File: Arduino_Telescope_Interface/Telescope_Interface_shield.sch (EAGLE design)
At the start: 30 parts, among them IC1 40106N, IC2 24LC256P, J1 RJ45, J11 455-1750-1-ND, J12 455-1750-1-ND, J4 455-1750-1-ND, J8 455-1750-1-ND, J9 455-1750-1-ND, SW2 MOMENTARY-SWITCH-SPST-PTH-6.0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

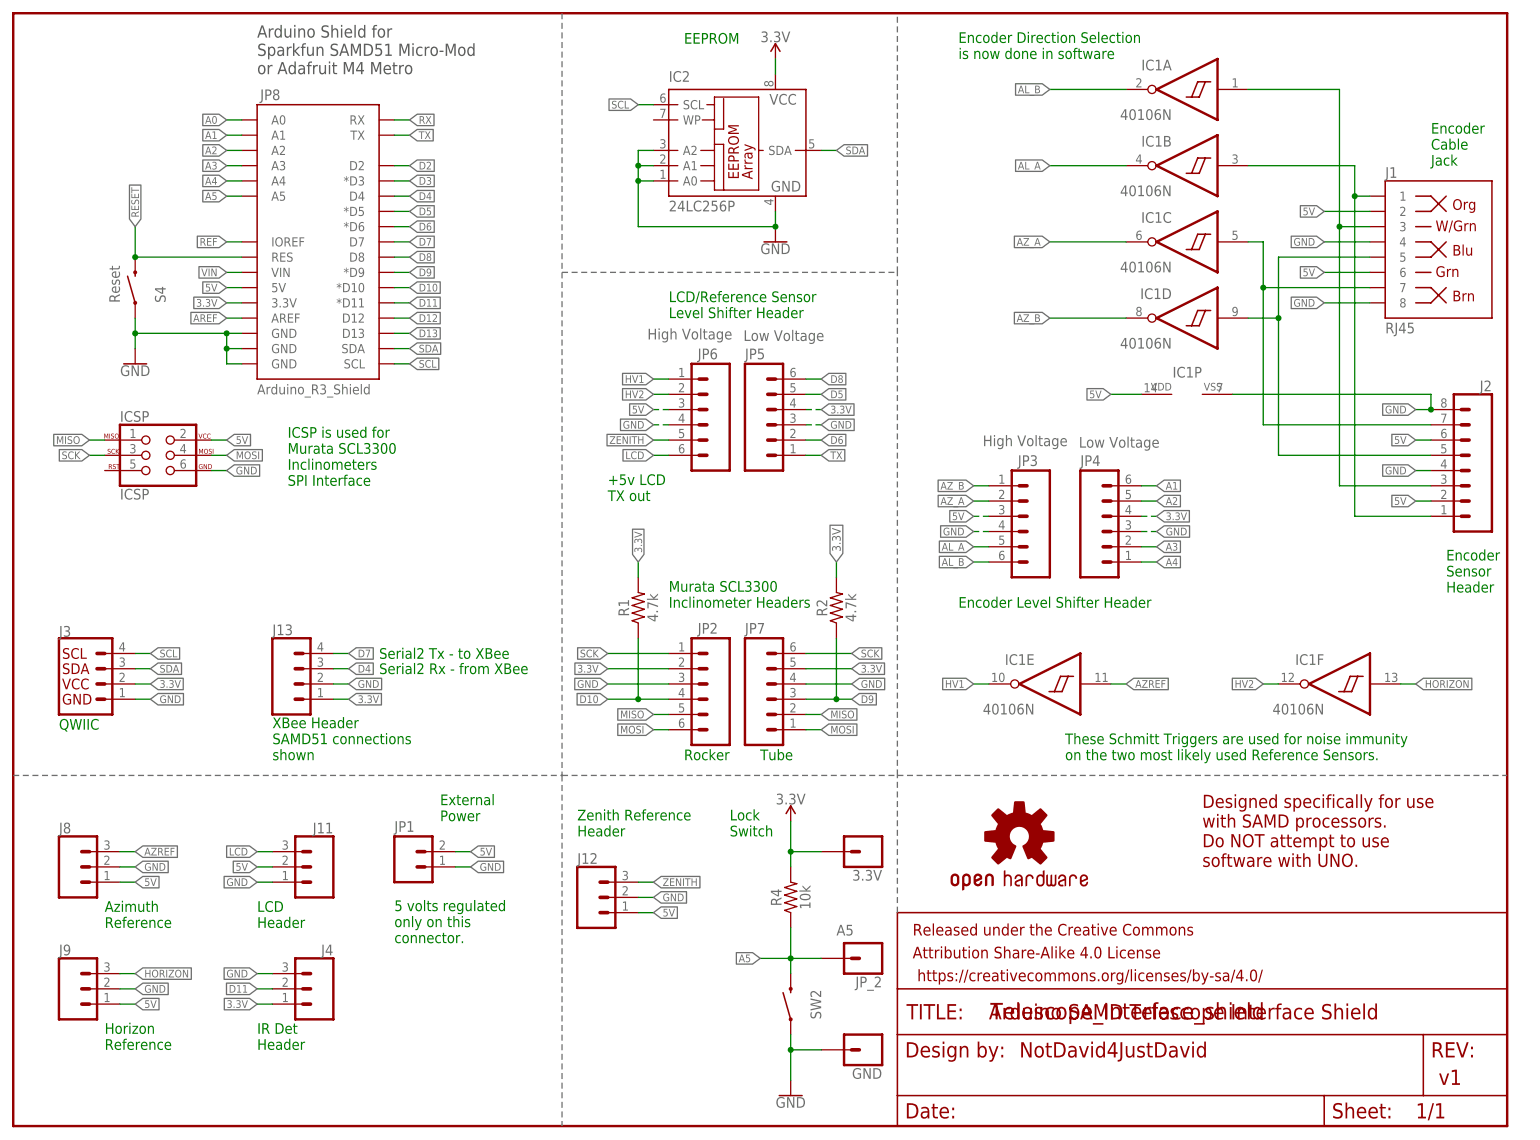
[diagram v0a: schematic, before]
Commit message: latest  changes in design, etc
Update design to separate out power monitoring.  Lots of other stuff too.
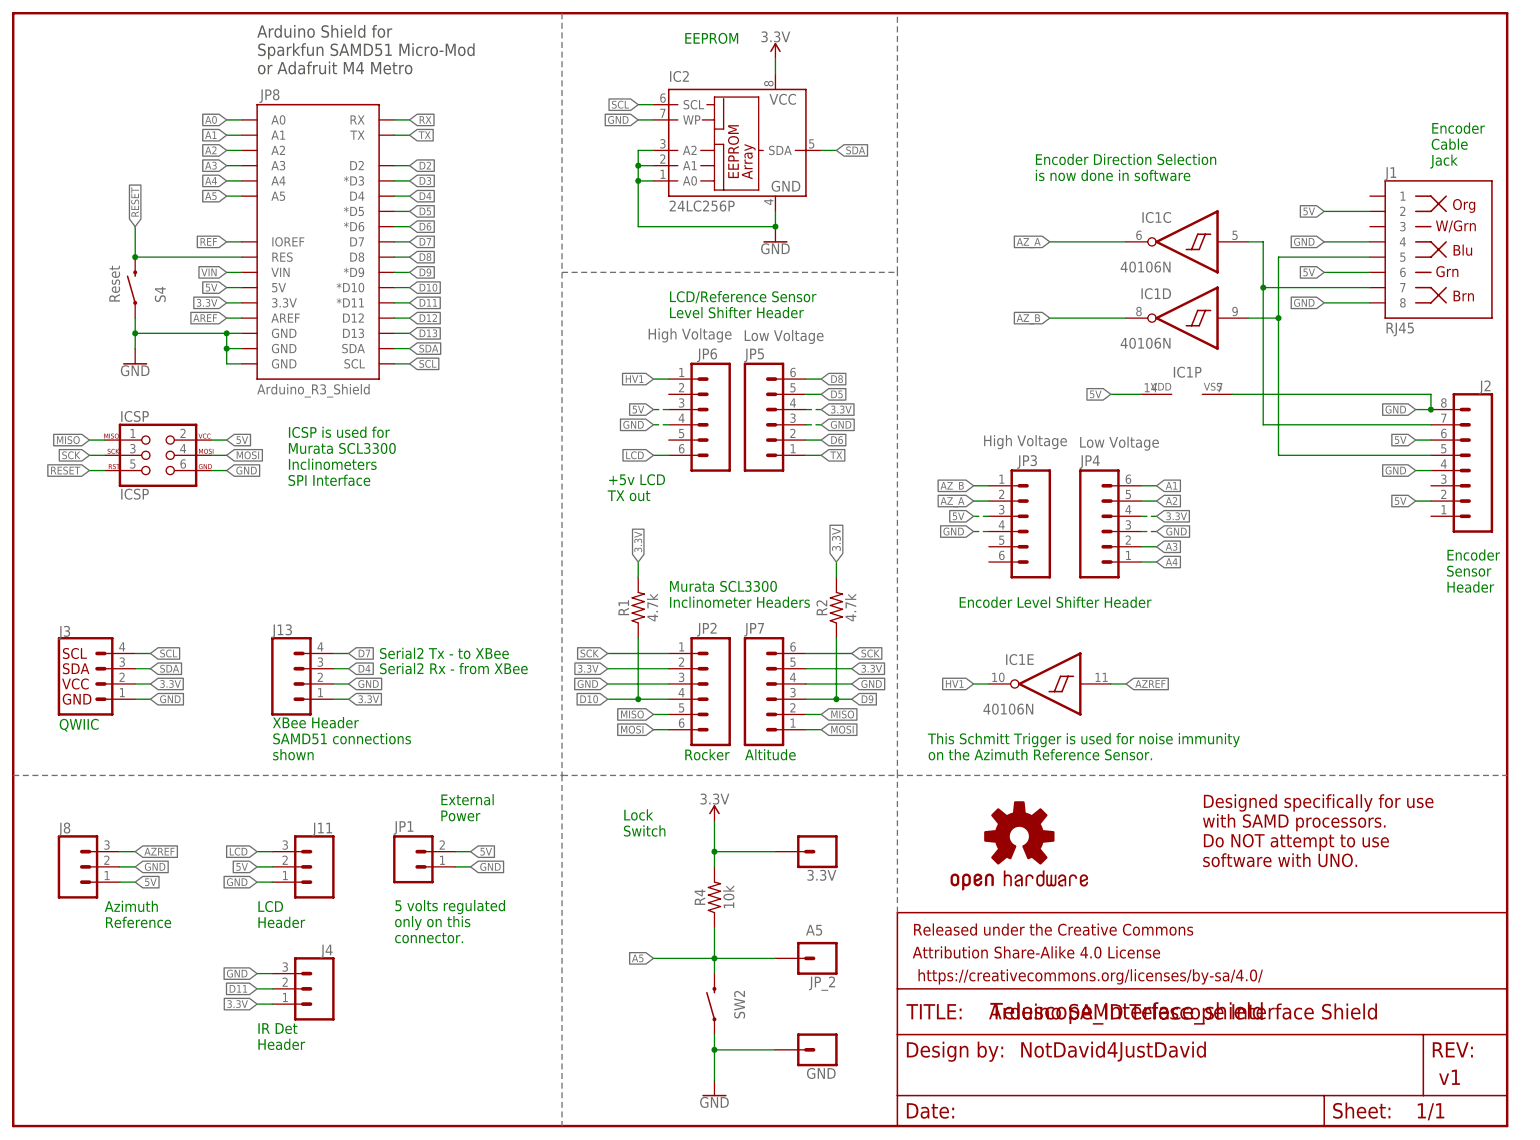
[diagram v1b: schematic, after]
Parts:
- removed J12, J9: 455-1750-1-ND, SparkFun-Connectors:CONN_03
- JP1: device SparkFun-Connectors:M02JST-PTH-2 -> SparkFun-Connectors:CONN_02JST-PTH-2
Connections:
- removed net AL_A: IC1B.O, JP3.5
- removed net AL_B: IC1A.O, JP3.6
- removed net HORIZON: IC1F.I, J9.3
- removed net HV2: IC1F.O, JP6.2
- removed net N$6: IC1B.I, J1.1, J2.1
- removed net N$7: IC1A.I, J1.3, J2.3
- removed net ZENITH: J12.3, JP6.5
- new net N$1: ICSP.5
- net 5V: no longer J12.1, J9.1
- net GND: now also IC2.WP; no longer J12.2, J9.2
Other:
- note added: "Altitude"
- note added: "This Schmitt Trigger is used for noise immunity on the Azimuth Reference Sensor."
- note removed: "Horizon Reference"
- note removed: "These Schmitt Triggers are used for noise immunity on the two most likely used Reference Sensors."
- note removed: "Tube"
- note removed: "Zenith Reference Header"
- moved on the sheet: 3.3V, GND, JP_2, R4, SW2
